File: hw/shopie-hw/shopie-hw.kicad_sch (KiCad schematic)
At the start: 41 parts, among them J1 Jack-DC, J2 USB_B_Micro, J3 Conn_01x04_Socket, SW1 SW_SPDT, SW2 SW_MEC_5E, SW3 SW_SPDT, U2 STM32F405RGT6, U3 LM2596T-5, U4 AP2112K-3.3, U6 MIC5365-1.8YC5, Y2 Crystal_Small

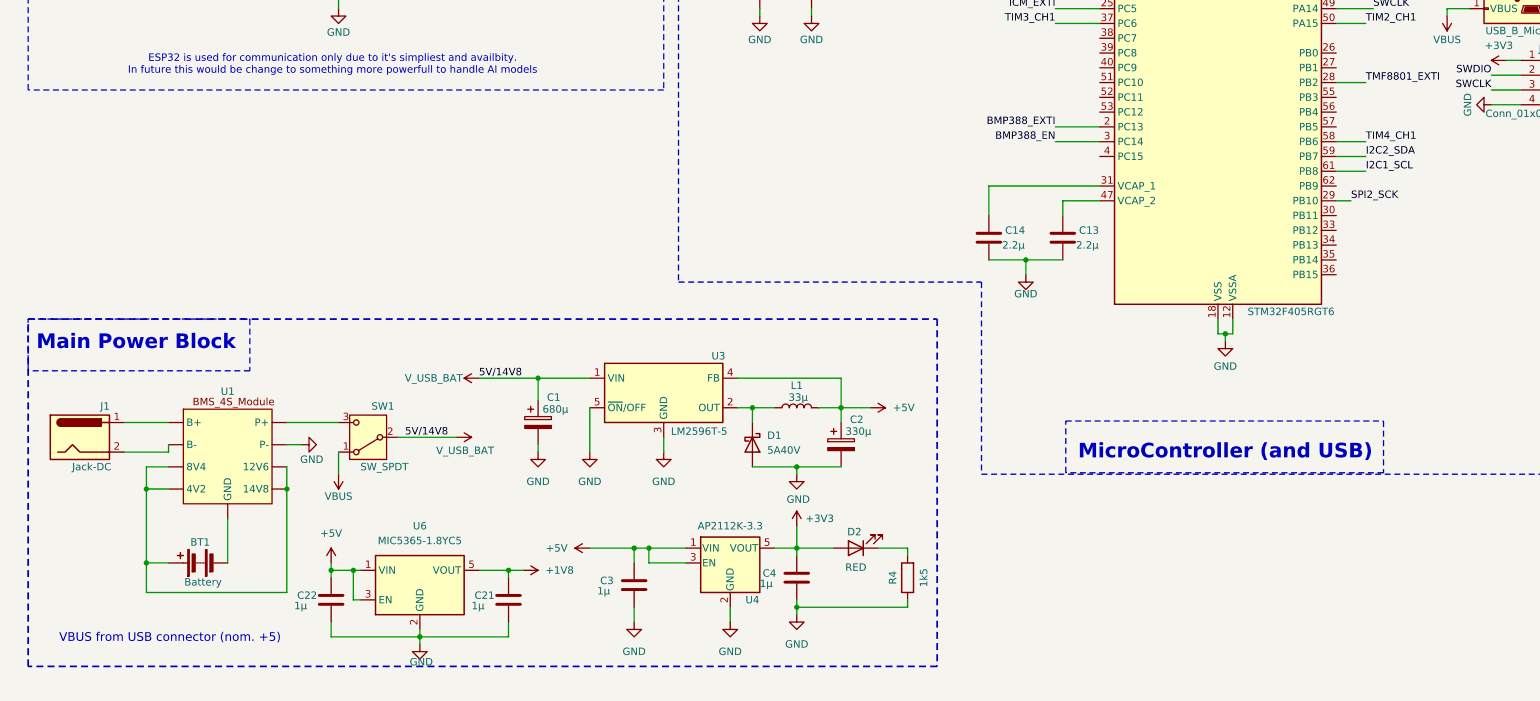
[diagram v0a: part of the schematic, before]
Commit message: Add LTC2943 battery fuel gauge
- Added LTC2943 current and voltage monitor IC to the schematic
- Connected LTC2943 SENSE+ and SENSE− pins to the 0.5mΩ, 9W shunt resistor terminals for current sensing
- Shunt resistor placed in high-side battery+ line for accurate current measurement
- Added I2C connections (SDA, SCL) to MCU
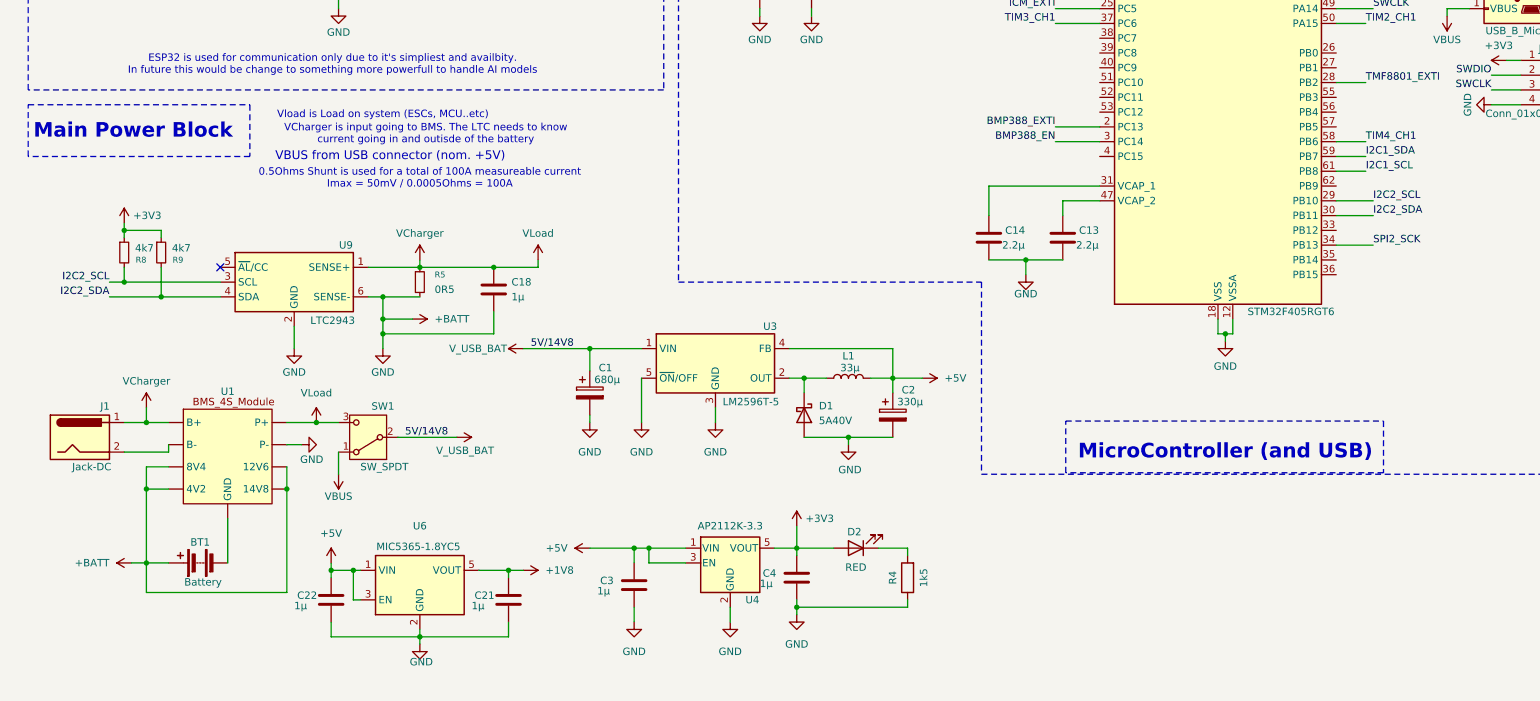
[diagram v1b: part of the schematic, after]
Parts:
- added C18: 1µ, symbol Device:C
- added R5: 0R5, symbol Device:R_Small
- added R8, R9: 4k7, symbol Device:R_Small
- added U9: LTC2943, Package_DFN_QFN:DFN-6-1EP_3x2mm_P0.5mm_EP1.65x1.35mm, symbol Battery_Management:LTC2942
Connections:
- net +3V3: now also R8.1, R9.1
- net I2C2_SDA: now also U2.30 (PB11), R9.2, U9.4 (SDA); no longer U2.59 (PB7)
- net SPI2_SCK: now also U2.34 (PB13); no longer U2.29 (PB10)
- net VCharger: now reaches J1.1, U1. (14V8)
- net VCharger: now also SW1.3 (C), C18.1, R5.1, U9.1 (SENSE+)
- net +BATT: now reaches BT1.1 (+), U1. (14V8)
- net +BATT: now also A1.29 (GND), A1.4 (GND), C1.2, C10.2, C11.2, C12.2, C13.2, C14.2, C15.2, C16.2, C17.2, C2.2, C21.2, C22.2, C3.2, C4.2, C5.2, C6.2, C7.2, C8.2, C9.2, D1.2 (A), J2.5 (GND), J3.4 (Pin_4), R4.1, SW3.1 (A), U2.12 (VSSA), U2.18 (VSS), U2.63 (VSS), U3.3 (GND), U3.5 (~{ON}/OFF), U4.2 (GND), U6.2 (GND), C18.2, R5.2, U9.2 (GND), U9.6 (SENSE-)
- removed net GND: A1.29 (GND), A1.4 (GND), C1.2, C10.2, C11.2, C12.2, C13.2, C14.2, C15.2, C16.2, C17.2, C2.2, C21.2, C22.2, C3.2, C4.2, C5.2, C6.2, C7.2, C8.2, C9.2, D1.2 (A), J2.5 (GND), J3.4 (Pin_4), R4.1, SW3.1 (A), U1. (14V8), U2.12 (VSSA), U2.18 (VSS), U2.63 (VSS), U3.3 (GND), U3.5 (~{ON}/OFF), U4.2 (GND), U6.2 (GND)
- new net I2C1_SDA: U2.59 (PB7)
- new net I2C2_SCL: R8.2, U2.29 (PB10), U9.3 (SCL)
- no-connect marks 2 -> 3
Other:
- note added: "0.5Ohms Shunt is used for a total of 100A measureable current Imax = 50mV / 0.0005Ohms = 100A"
- note added: "VBUS from USB connector (nom. +5V)"
- note added: "VCharger is input going to BMS. The LTC needs to know current going in and outisde of the battery"
- note added: "Vload is Load on system (ESCs, MCU..etc)"
- note removed: "VBUS from USB connector (nom. +5)"
- moved on the sheet: C1, C2, D1, L1, U3

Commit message: Add ESC symbol and complete schematic connections, Update MCU pinout
- Created custom KiCad symbol for the HAKRC BLHeli_32 40A 4-in-1 ESC
- Connected ESC signal lines to MCU PWM outputs, CURR to ADC, and TX to UART RX
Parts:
- removed A1: Arduino_Nano_ESP32, Module:Arduino_Nano, symbol MCU_Module:Arduino_Nano_ESP32
- removed BT1: Battery, symbol Device:Battery
- removed C1: 680µ, symbol Device:C_Polarized
- removed C10, C15, C5, C6, C7, C8: 100n, symbol Device:C
- removed C11, C12, C18, C21, C22, C3, C4: 1µ, symbol Device:C
- removed C13, C14: 2.2µ, symbol Device:C
- removed C16, C17: 30p, symbol Device:C
- removed C2: 330µ, symbol Device:C_Polarized
- removed C9: 4.7µ, symbol Device:C
- removed D1: 5A40V, symbol Device:D_Schottky
- removed D2: RED, symbol Device:LED
- removed FB1: 100R, symbol Device:FerriteBead
- removed J1: Jack-DC, symbol Connector:Jack-DC
- removed J2: USB_B_Micro, symbol Connector:USB_B_Micro
- removed J3: Conn_01x04_Socket, symbol Connector:Conn_01x04_Socket
- removed L1: 33µ, symbol Device:L
- removed R1: 10kR, symbol Device:R
- removed R2: 10k, symbol Device:R
- removed R3, R4: 1k5, symbol Device:R
- removed R5: 0R5, symbol Device:R_Small
- removed R8, R9: 4k7, symbol Device:R_Small
- removed SW1, SW3: SW_SPDT, symbol Switch:SW_SPDT
- removed SW2: SW_MEC_5E, symbol Switch:SW_MEC_5E
- removed U1: ~, symbol shopie-hwLibrary:BMS_4S_Module
- removed U2: STM32F405RGT6, Package_QFP:LQFP-64_10x10mm_P0.5mm, symbol MCU_ST_STM32F4:STM32F405RGTx
- removed U3: LM2596T-5, Package_TO_SOT_THT:TO-220-5_P3.4x3.7mm_StaggerOdd_Lead3.8mm_Vertical, symbol Regulator_Switching:LM2596T-5
- removed U4: AP2112K-3.3, Package_TO_SOT_SMD:SOT-23-5, symbol Regulator_Linear:AP2112K-3.3
- removed U6: MIC5365-1.8YC5, Package_TO_SOT_SMD:SOT-353_SC-70-5, symbol Regulator_Linear:MIC5365-1.8YC5
- removed U9: LTC2943, Package_DFN_QFN:DFN-6-1EP_3x2mm_P0.5mm_EP1.65x1.35mm, symbol Battery_Management:LTC2942
- removed Y2: Crystal_Small, symbol Device:Crystal_Small
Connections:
- no-connect marks 3 -> 0
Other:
- sheet MCU, Power, Communication renamed Sensors and Perhperials
- added sheet MCU,Power,Comm (Main.kicad_sch)
- note removed: "0.5Ohms Shunt is used for a total of 100A measureable current Imax = 50mV / 0.0005Ohms = 100A"
- note removed: "1x 100nF per VDD pin + Bukk cap 4.7uF"
- note removed: "Communication"
- note removed: "ESP32 is used for communication only due to it's simpliest and availbity. In future this would be change to something more powerfull to handle AI models"
- note removed: "Main Power Block"
- note removed: "MicroController (and USB)"
- note removed: "Reset Switch"
- note removed: "USB App note AN4879"
- note removed: "VBUS from USB connector (nom. +5V)"
- note removed: "VCharger is input going to BMS. The LTC needs to know current going in and outisde of the battery"
- note removed: "VDDA Filtering"
- note removed: "Vload is Load on system (ESCs, MCU..etc)"

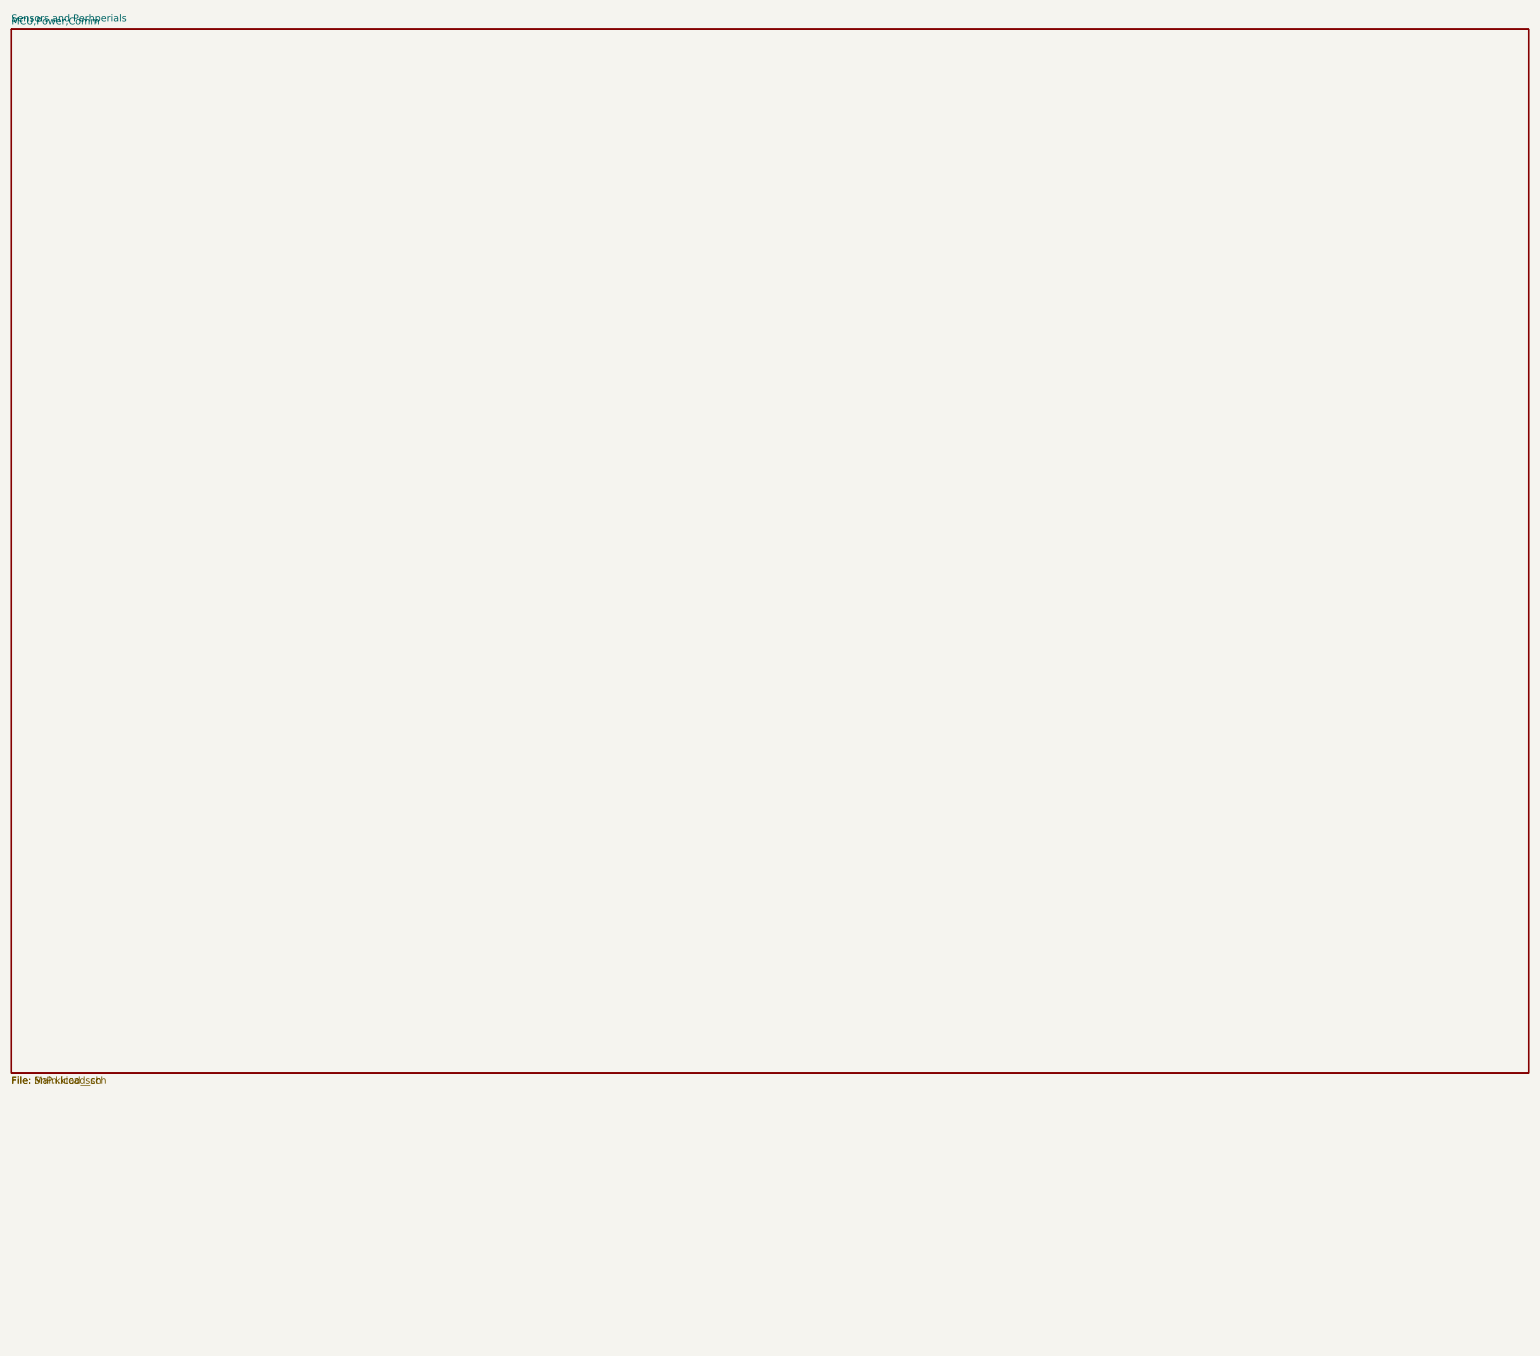
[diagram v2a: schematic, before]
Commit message: Fix most ERC Errors and Connect hierarchical labels across schematic pages
- Connected missing net labels across MCU, Sensors, and Power pages
- Final ERC check passed with no errors or warnings for all labels
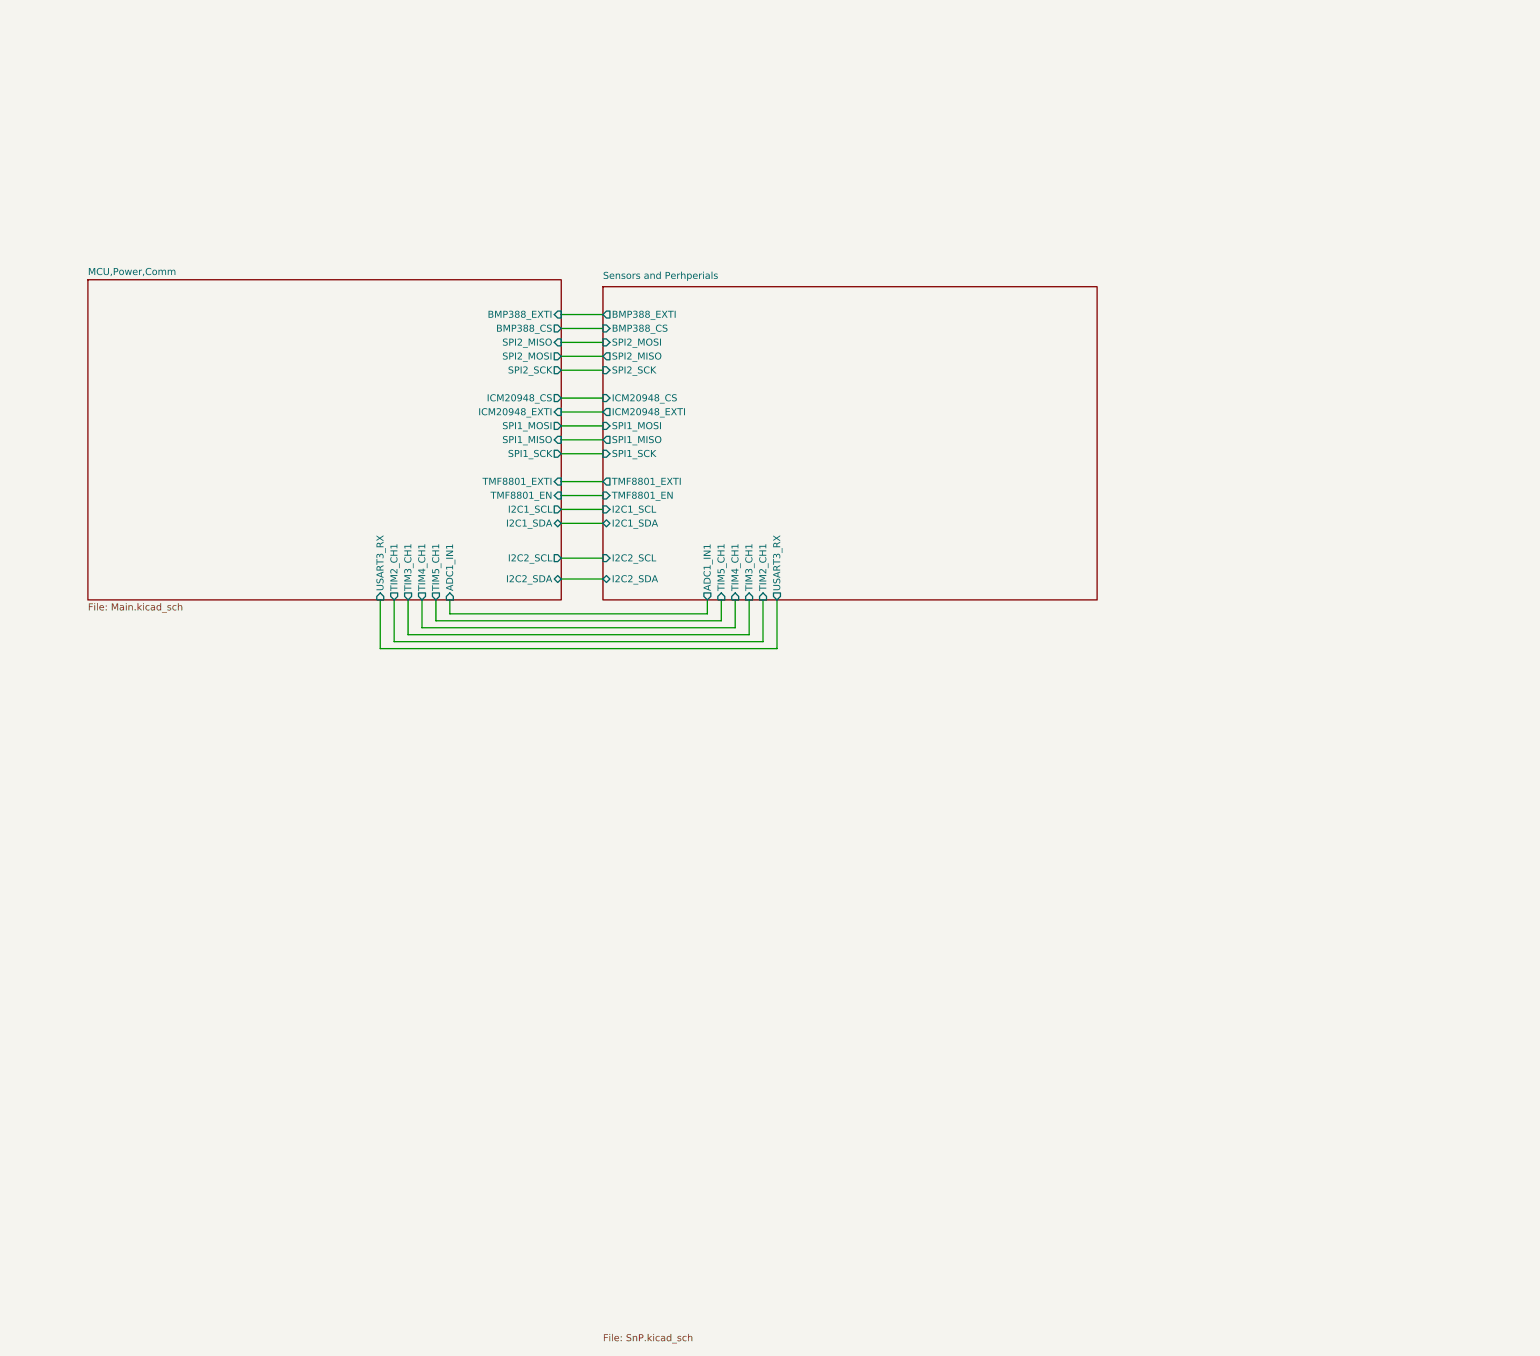
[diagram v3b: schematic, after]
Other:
- sheet MCU,Power,Comm ports: added ADC1_IN1, BMP388_CS, BMP388_EXTI, I2C1_SCL, I2C1_SDA, I2C2_SCL, I2C2_SDA, ICM20948_CS, ICM20948_EXTI, SPI1_MISO, SPI1_MOSI, SPI1_SCK, SPI2_MISO, SPI2_MOSI, SPI2_SCK, TIM2_CH1, TIM3_CH1, TIM4_CH1, TIM5_CH1, TMF8801_EN, TMF8801_EXTI, USART3_RX; removed none
- sheet Sensors and Perhperials ports: added ADC1_IN1, BMP388_CS, BMP388_EXTI, I2C1_SCL, I2C1_SDA, I2C2_SCL, I2C2_SDA, ICM20948_CS, ICM20948_EXTI, SPI1_MISO, SPI1_MOSI, SPI1_SCK, SPI2_MISO, SPI2_MOSI, SPI2_SCK, TIM2_CH1, TIM3_CH1, TIM4_CH1, TIM5_CH1, TMF8801_EN, TMF8801_EXTI, USART3_RX; removed none
